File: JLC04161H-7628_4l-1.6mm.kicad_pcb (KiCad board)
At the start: 4 copper layers, 24 x 24 mm, 0 parts

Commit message: add default zone
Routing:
- added copper zone on F.Cu, net (none)
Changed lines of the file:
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@@
 		(layer "Edge.Cuts")
 	)
+	(zone
+		(net 0)
+		(net_name "")
+		(layer "F.Cu")
+		(hatch edge 0.5)
+		(connect_pads
+			(clearance 0.127)
+		)
+		(min_thickness 0.127)
+		(filled_areas_thickness no)
+		(fill
+			(thermal_gap 0.127)
+			(thermal_bridge_width 0.5)
+			(smoothing fillet)
+			(radius 1)
+			(island_removal_mode 1)
+			(island_area_min 10)
+		)
+		(polygon
+			(pts
+				(xy 29 29) (xy 55 29) (xy 55 55) (xy 29 55)
+			)
+		)
+	)
 )

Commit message: update
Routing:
- added copper zone on B.Cu, net (none)
- added copper zone on In1.Cu, net (none)
- added copper zone on In2.Cu, net (none)
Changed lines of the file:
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@@
 			(layer "dielectric 1"
 				(type "prepreg")
-				(thickness 0.2030 locked)
+				(thickness 0.203 locked)
 				(material "7628")
 				(epsilon_r 4.4)
@@
 			(layer "dielectric 3"
 				(type "prepreg")
-				(thickness 0.2030 locked)
+				(thickness 0.203 locked)
 				(material "7628")
 				(epsilon_r 4.4)
@@
 		(net 0)
 		(net_name "")
-		(layer "F.Cu")
+		(layers "F&B.Cu")
 		(hatch edge 0.5)
 		(connect_pads
@@
 			)
 		)
+	)
+	(zone
+		(net 0)
+		(net_name "")
+		(layers "In1.Cu" "In2.Cu")
+		(hatch edge 0.5)
+		(priority 1)
+		(connect_pads
+			(clearance 0.2)
+		)
+		(min_thickness 0.2)
+		(filled_areas_thickness no)
+		(fill
+			(thermal_gap 0.2)
+			(thermal_bridge_width 0.5)
+			(smoothing fillet)
+			(radius 1)
+			(island_removal_mode 1)
+			(island_area_min 10)
+		)
+		(polygon
+			(pts
+				(xy 28 28) (xy 56 28) (xy 56 56) (xy 28 56)
+			)
+		)

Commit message: update silk
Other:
- board text added: "JLCJLCJLCJLC"
- board text added: "TES"
- board text added: "VERV"
- board text added: "test test test"
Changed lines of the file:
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@@
 	(net 0 "")
+	(gr_line
+		(start 48.999999 38.124999)
+		(end 49 35.875)
+		(stroke
+			(width 0.1)
+			(type default)
+		)
+		(layer "F.SilkS")
+	)
+	(gr_rect
+		(start 38 40)
+		(end 43 45)
+		(stroke
+			(width 0.1)
+			(type solid)
+		)
+		(fill solid)
+		(layer "F.SilkS")
+	)
+	(gr_line
+		(start 48.999999 38.124999)
+		(end 46.750001 38.124998)
+		(stroke
+			(width 0.1)
+			(type default)
+		)
+		(layer "F.SilkS")
+	)
+	(gr_line
+		(start 46.75 35.874999)
+		(end 46.750001 38.124998)
+		(stroke
+			(width 0.1)
+			(type default)
+		)
+		(layer "F.SilkS")
+	)
+	(gr_line
+		(start 49 35.875)
+		(end 46.75 35.874999)
+		(stroke
+			(width 0.1)
+			(type default)
+		)
+		(layer "F.SilkS")
+	)
 	(gr_line
 		(start 30 31)
@@
 		)
 		(layer "Edge.Cuts")
+	)
+	(gr_text "VERV"
+		(at 46 36.624999 0)
+		(layer "F.SilkS")
+		(effects
+			(font
+				(size 0.8 0.8)
+				(thickness 0.15)
+				(bold yes)
+				(italic yes)
+			)
+			(justify right)
+		)
+	)
+	(gr_text "TES"
+		(at 37.75 36.5 0)
+		(layer "F.SilkS")
+		(effects
+			(font
+				(size 1 1)
+				(thickness 0.2)
+				(bold yes)
+				(italic yes)
+			)
+			(justify left)
+		)
+	)
+	(gr_text "test test test"
+		(at 37.75 37.749999 0)
+		(layer "F.SilkS")
+		(effects
+			(font
+				(size 0.8 0.8)
+				(thickness 0.15)
+				(bold yes)
+			)
+			(justify left)
+		)
+	)
+	(gr_text "JLCJLCJLCJLC"
+		(at 42 46 0)
+		(layer "F.SilkS")
+		(effects
+			(font
+				(size 0.8 0.8)
+				(thickness 0.15)
+			)
+		)
+	)
+	(dimension
+		(type aligned)
+		(layer "Dwgs.User")
+		(pts
+			(xy 49.999999 54.000001) (xy 50 30)
+		)
+		(height 7.999999)
+		(gr_text "24,0000 mm"
+			(at 56.849999 42 89.99999523)
+			(layer "Dwgs.User")
+			(effects
+				(font
+					(size 1 1)
+					(thickness 0.15)
+				)
+			)
+		)
+		(format
+			(prefix "")
+			(suffix "")
+			(units 3)
+			(units_format 1)
+			(precision 4)
+		)
+		(style
+			(thickness 0.1)
+			(arrow_length 1.27)
+			(text_position_mode 0)
+			(extension_height 0.58642)
+			(extension_offset 0.5) keep_text_aligned)
+	)
+	(dimension
+		(type aligned)
+		(layer "Dwgs.User")
+		(pts
+			(xy 30 50) (xy 54 50)
+		)
+		(height 7.999999)
+		(gr_text "24,0000 mm"
+			(at 42 56.849999 0)
+			(layer "Dwgs.User")
+			(effects
+				(font
+					(size 1 1)
+					(thickness 0.15)
+				)
+			)
+		)
+		(format
+			(prefix "")
+			(suffix "")
+			(units 3)
+			(units_format 1)
+			(precision 4)
+		)
+		(style
+			(thickness 0.1)
+			(arrow_length 1.27)
+			(text_position_mode 0)
+			(extension_height 0.58642)
+			(extension_offset 0.5) keep_text_aligned)
 	)
 	(zone
@@
 		)
 	)
+	(group ""
+		(members "3ebb9490-2b51-4eec-9b5c-cec9ce23fb9a" "7fb9661b-84d3-442d-a015-0e268f022289"
+			"d70f0362-5fd3-4c70-8296-c3f0b773bed5" "f644a623-07d3-48f7-8d47-325abe88bbbc"
+		)
+	)
+	(group ""
+		(members "3effe912-0202-4894-a594-ea1e9639254b")
+	)
+	(group ""
+		(members "2b661437-7d18-4828-9fe4-5bc542f32afd" "4193ec86-0c5a-406a-9112-550daa1af96e"
+			"5663adf4-a367-4757-9f2c-ed05ab274832"
+		)
+	)

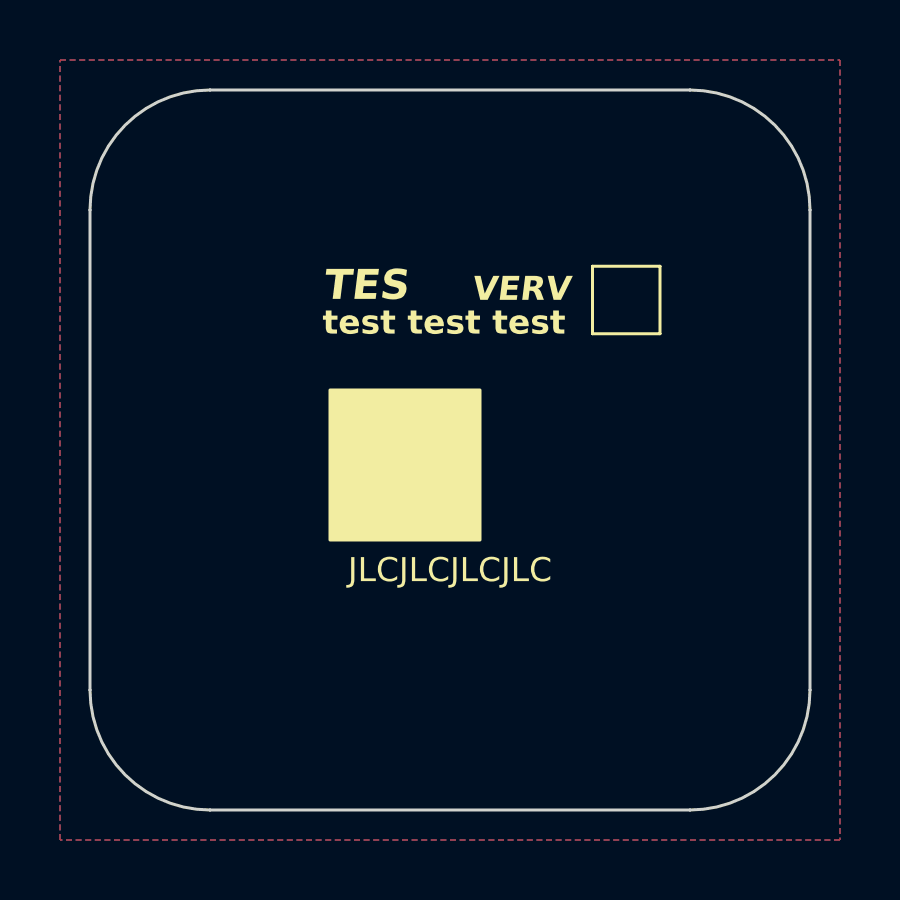
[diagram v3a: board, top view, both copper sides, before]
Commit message: Update to kicad9
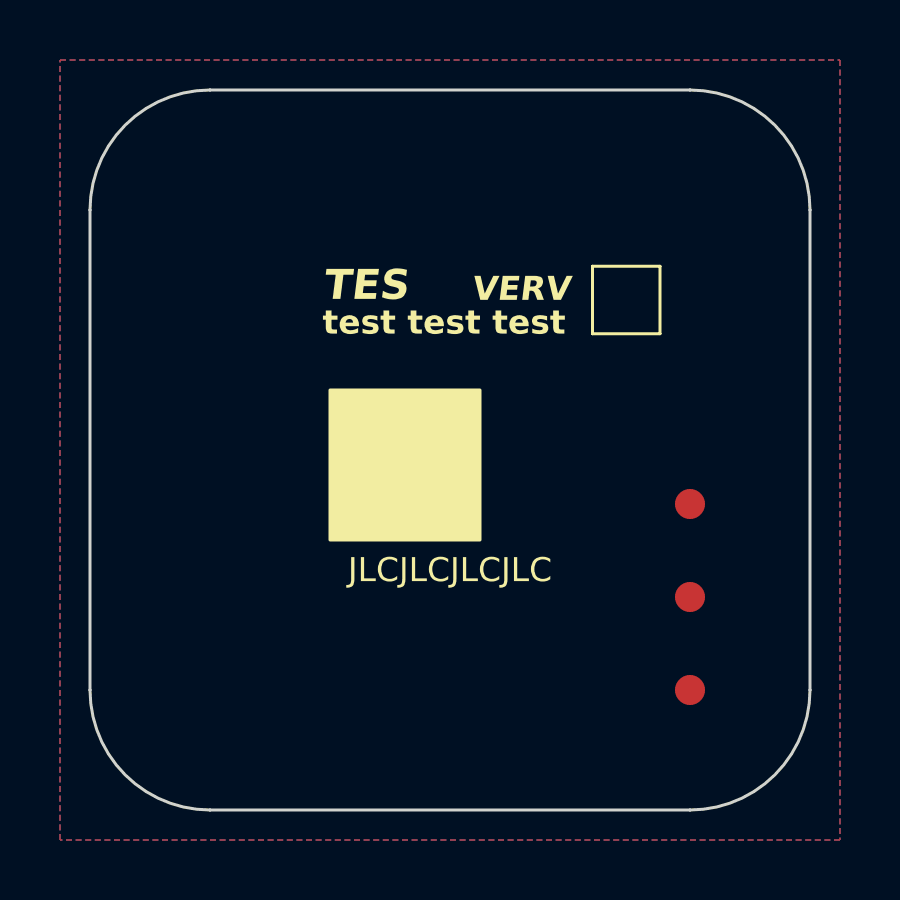
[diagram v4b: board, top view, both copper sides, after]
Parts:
- added FID1: Fiducial, MAS_Package_std:Fiducial_1mm_Mask2mm, F.Cu at (50.0, 43.8)
- added FID2: Fiducial, MAS_Package_std:Fiducial_1mm_Mask2mm, F.Cu at (50.0, 46.9)
- added FID3: Fiducial, MAS_Package_std:Fiducial_1mm_Mask2mm, F.Cu at (50.0, 50.0)
